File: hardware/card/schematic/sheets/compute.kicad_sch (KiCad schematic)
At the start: 5 parts, among them U1 ESP32-P4-Module-32MB

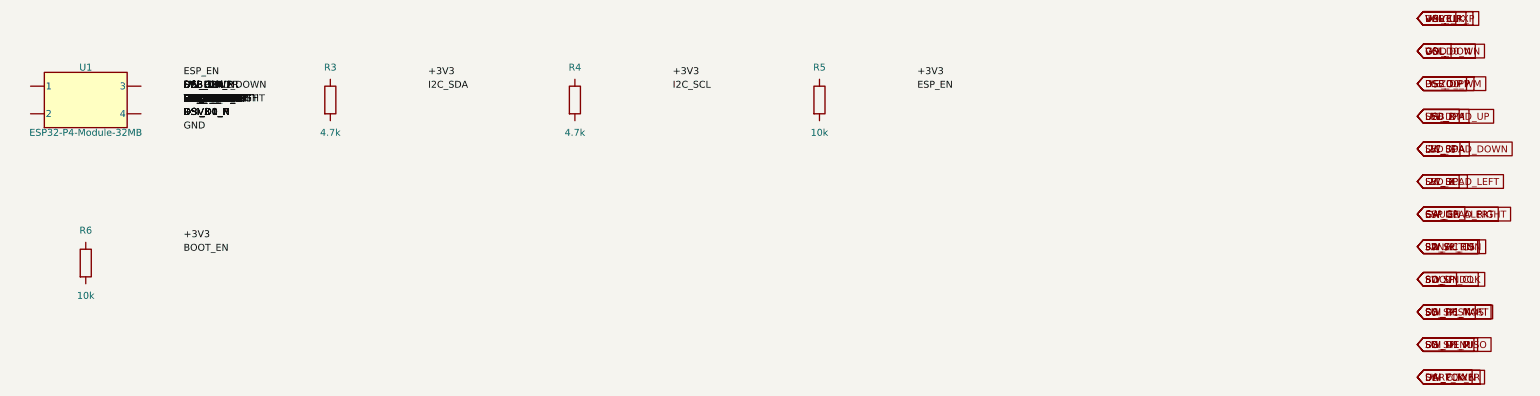
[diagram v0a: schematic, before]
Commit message: hardware: replace U7 power latch with a slide switch (hard off)
Owner-approved power model: top-edge SPDT slide switch gates the TPS63070
EN pin; hard off is the normal off (Game Boy/Arduboy style, ~1-1.5 s tuned
cold boot, end-of-level atomic saves). Deletes the U7 latch IC and SYSOFF
wiring, frees GPIO8, adds a VBUS-powered charge LED on BQ24075 CHG, and
demotes deep sleep to an optional idle battery-saver. Closes the U7
pre-route gate from the 2026-07-09 PCB review.

Co-authored-by: Cursor <cursoragent@cursor.com>
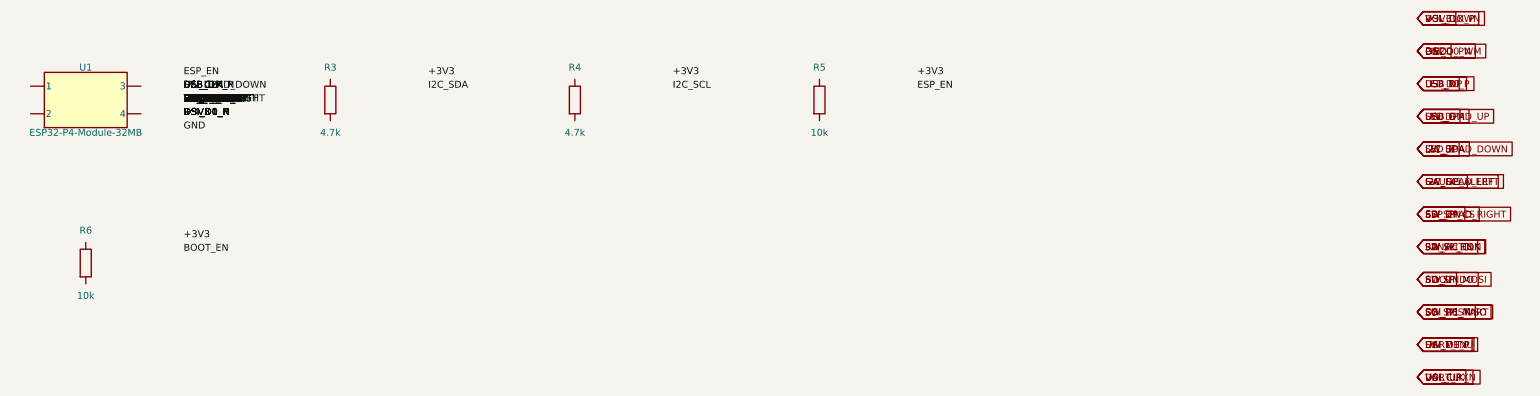
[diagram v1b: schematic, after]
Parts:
- removed R3: 4.7k, 0402, symbol Device:R
- added R6: 10k, 0402, symbol Device:R
- R4: renamed from R5; value 10k -> 4.7k
- renumbered R4 to R3, R6 to R5
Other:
- moved on the sheet: R3, R4, R5
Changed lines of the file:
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@@
   (title_block
     (title "PuzzleScript Card — compute")
-    (date "2026-07-08")
+    (date "2026-07-09")
     (rev "spin1")
     (comment 1 "Auto-generated from connectivity.json")
@@
   (label "SW_MENU" (at 53 35 0) (fields_autoplaced)
     (effects (font (size 1.27 1.27)) (justify left)))
-  (label "SW_POWER" (at 53 32.5 0) (fields_autoplaced)
-    (effects (font (size 1.27 1.27)) (justify left)))
   (label "VOL_UP" (at 53 35 0) (fields_autoplaced)
     (effects (font (size 1.27 1.27)) (justify left)))
@@
       (effects (font (size 1.27 1.27)) hide))
   )
-  (global_label "SW_POWER" (shape input) (at 280 86 0) (fields_autoplaced)
+  (global_label "VOL_UP" (shape input) (at 280 86 0) (fields_autoplaced)
     (effects (font (size 1.27 1.27)) (justify left))
     (property "Intersheetrefs" "${INTERSHEET_REFS}" (at 280 86 0)
       (effects (font (size 1.27 1.27)) hide))
   )
-  (global_label "VOL_UP" (shape input) (at 280 20 0) (fields_autoplaced)
+  (global_label "VOL_DOWN" (shape input) (at 280 20 0) (fields_autoplaced)
     (effects (font (size 1.27 1.27)) (justify left))
     (property "Intersheetrefs" "${INTERSHEET_REFS}" (at 280 20 0)
       (effects (font (size 1.27 1.27)) hide))
   )
-  (global_label "VOL_DOWN" (shape input) (at 280 26 0) (fields_autoplaced)
+  (global_label "PIEZO_PWM" (shape input) (at 280 26 0) (fields_autoplaced)
     (effects (font (size 1.27 1.27)) (justify left))
     (property "Intersheetrefs" "${INTERSHEET_REFS}" (at 280 26 0)
       (effects (font (size 1.27 1.27)) hide))
   )
-  (global_label "PIEZO_PWM" (shape input) (at 280 32 0) (fields_autoplaced)
+  (global_label "LED_R" (shape input) (at 280 32 0) (fields_autoplaced)
     (effects (font (size 1.27 1.27)) (justify left))
     (property "Intersheetrefs" "${INTERSHEET_REFS}" (at 280 32 0)
       (effects (font (size 1.27 1.27)) hide))
   )
-  (global_label "LED_R" (shape input) (at 280 38 0) (fields_autoplaced)
+  (global_label "LED_G" (shape input) (at 280 38 0) (fields_autoplaced)
     (effects (font (size 1.27 1.27)) (justify left))
     (property "Intersheetrefs" "${INTERSHEET_REFS}" (at 280 38 0)
       (effects (font (size 1.27 1.27)) hide))
   )
-  (global_label "LED_G" (shape input) (at 280 44 0) (fields_autoplaced)
+  (global_label "LED_B" (shape input) (at 280 44 0) (fields_autoplaced)
     (effects (font (size 1.27 1.27)) (justify left))
     (property "Intersheetrefs" "${INTERSHEET_REFS}" (at 280 44 0)
       (effects (font (size 1.27 1.27)) hide))
   )
-  (global_label "LED_B" (shape input) (at 280 50 0) (fields_autoplaced)
+  (global_label "GAUGE_ALERT" (shape input) (at 280 50 0) (fields_autoplaced)
     (effects (font (size 1.27 1.27)) (justify left))
     (property "Intersheetrefs" "${INTERSHEET_REFS}" (at 280 50 0)
       (effects (font (size 1.27 1.27)) hide))
   )
-  (global_label "GAUGE_ALERT" (shape input) (at 280 56 0) (fields_autoplaced)
+  (global_label "SD_SPI_CS" (shape input) (at 280 56 0) (fields_autoplaced)
     (effects (font (size 1.27 1.27)) (justify left))
     (property "Intersheetrefs" "${INTERSHEET_REFS}" (at 280 56 0)
       (effects (font (size 1.27 1.27)) hide))
   )
-  (global_label "SD_SPI_CS" (shape input) (at 280 62 0) (fields_autoplaced)
+  (global_label "SD_SPI_CLK" (shape input) (at 280 62 0) (fields_autoplaced)
     (effects (font (size 1.27 1.27)) (justify left))
     (property "Intersheetrefs" "${INTERSHEET_REFS}" (at 280 62 0)
       (effects (font (size 1.27 1.27)) hide))
   )
-  (global_label "SD_SPI_CLK" (shape input) (at 280 68 0) (fields_autoplaced)
+  (global_label "SD_SPI_MOSI" (shape input) (at 280 68 0) (fields_autoplaced)
     (effects (font (size 1.27 1.27)) (justify left))
     (property "Intersheetrefs" "${INTERSHEET_REFS}" (at 280 68 0)
       (effects (font (size 1.27 1.27)) hide))
   )
-  (global_label "SD_SPI_MOSI" (shape input) (at 280 74 0) (fields_autoplaced)
+  (global_label "SD_SPI_MISO" (shape input) (at 280 74 0) (fields_autoplaced)
     (effects (font (size 1.27 1.27)) (justify left))
     (property "Intersheetrefs" "${INTERSHEET_REFS}" (at 280 74 0)
       (effects (font (size 1.27 1.27)) hide))
   )
-  (global_label "SD_SPI_MISO" (shape input) (at 280 80 0) (fields_autoplaced)
+  (global_label "UART_TX" (shape input) (at 280 80 0) (fields_autoplaced)
     (effects (font (size 1.27 1.27)) (justify left))
     (property "Intersheetrefs" "${INTERSHEET_REFS}" (at 280 80 0)
       (effects (font (size 1.27 1.27)) hide))
   )
-  (global_label "UART_TX" (shape input) (at 280 86 0) (fields_autoplaced)
+  (global_label "UART_RX" (shape input) (at 280 86 0) (fields_autoplaced)
     (effects (font (size 1.27 1.27)) (justify left))
     (property "Intersheetrefs" "${INTERSHEET_REFS}" (at 280 86 0)
       (effects (font (size 1.27 1.27)) hide))
   )
-  (global_label "UART_RX" (shape input) (at 280 20 0) (fields_autoplaced)
-    (effects (font (size 1.27 1.27)) (justify left))
-    (property "Intersheetrefs" "${INTERSHEET_REFS}" (at 280 20 0)
-      (effects (font (size 1.27 1.27)) hide))
-  )

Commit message: hardware: go chip-down ESP32-P4NRW32X, drop WiFi, close display Z-stack
Owner-approved reversal of the module-for-spin-1 decision: the Waveshare
module is 3.3 mm tall, which fails the 9.5 mm display-zone stack (~10.5 mm),
and its C6 radio would ship dark since v1 needs no WiFi. Bare QFN104 chip
(0.9 mm) closes the stack at ~8.2 mm. Adds flash/crystal/DC-DC support
parts to connectivity (copied from the Espressif reference design at
capture), shrinks the back compute keep-out to a 20x20 chip-down cluster,
strips module castellation pin numbers from the pin budget, and records
both Z-stack closure tables in the spec. BOM must use the X silicon
revision (plain NRW32 is EOL).

Co-authored-by: Cursor <cursoragent@cursor.com>
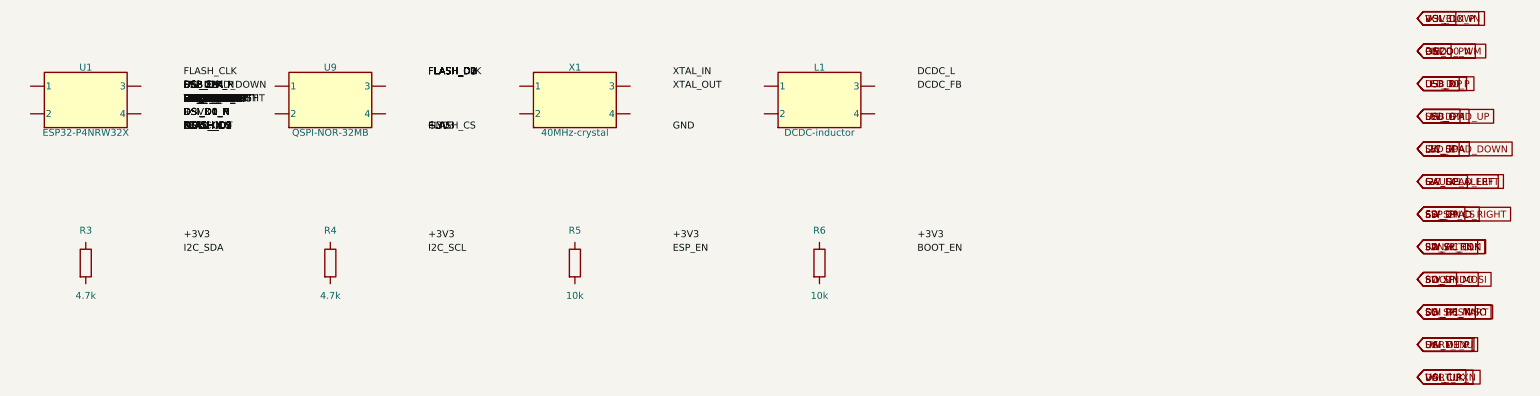
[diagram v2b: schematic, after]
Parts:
- added L1: DCDC-inductor, TBD, symbol PSCard:Block2
- added R6: 10k, 0402, symbol Device:R
- added X1: 40MHz-crystal, TBD, symbol PSCard:Block2
- U1: value ESP32-P4-Module-32MB -> ESP32-P4NRW32X; footprint Waveshare-ESP32-P4-Module -> QFN104-10x10-P0.35
- U9: renamed from R6; value 10k -> QSPI-NOR-32MB; footprint 0402 -> TBD; symbol Device:R -> PSCard:Block2
